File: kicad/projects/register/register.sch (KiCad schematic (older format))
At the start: 21 parts, among them J1 LEFT IN, J10 RIGHT LEDS, J2 LEFT OUT, J3 LEFT CONTENT, J4 BUS, J5 LEFT LEDS, J6 BACKPLANE, J7 RIGHT IN, J8 RIGHT OUT, J9 RIGHT CONTENT, U1 74HCT377, U2 74HCT245, U3 74HCT04, U4 74HCT377, U5 74HCT245

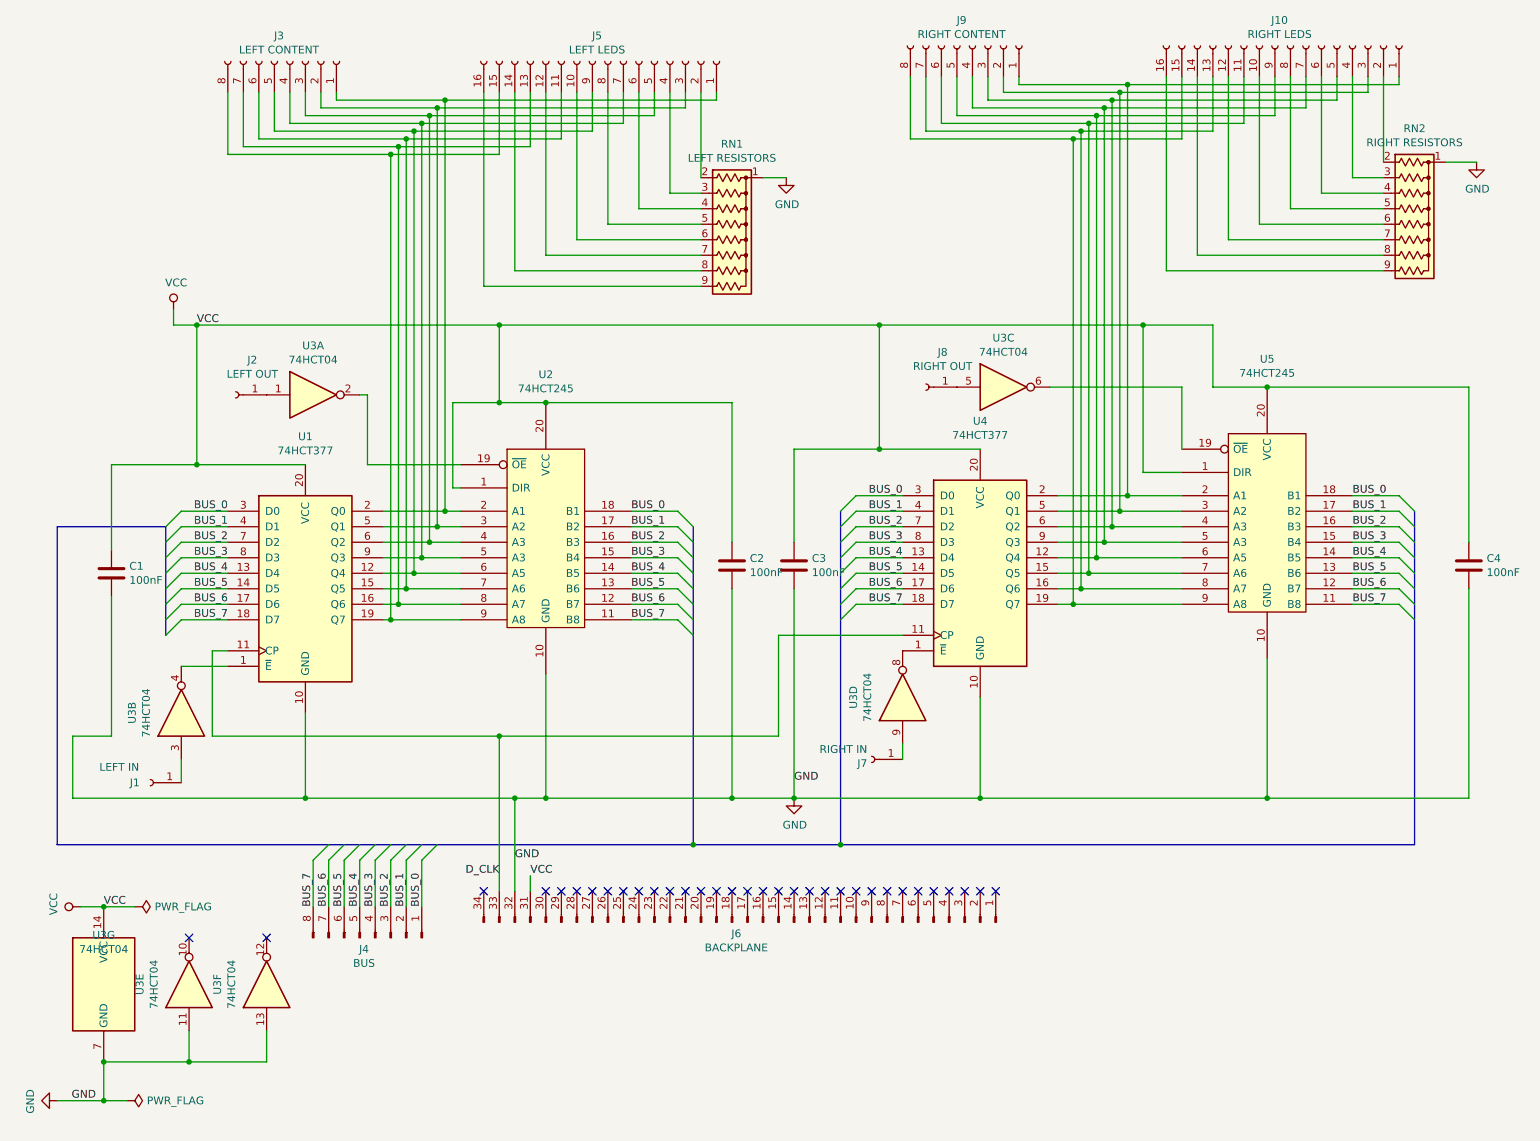
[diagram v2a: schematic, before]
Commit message: First version of register pcb. Ground and power planes giving poor results.
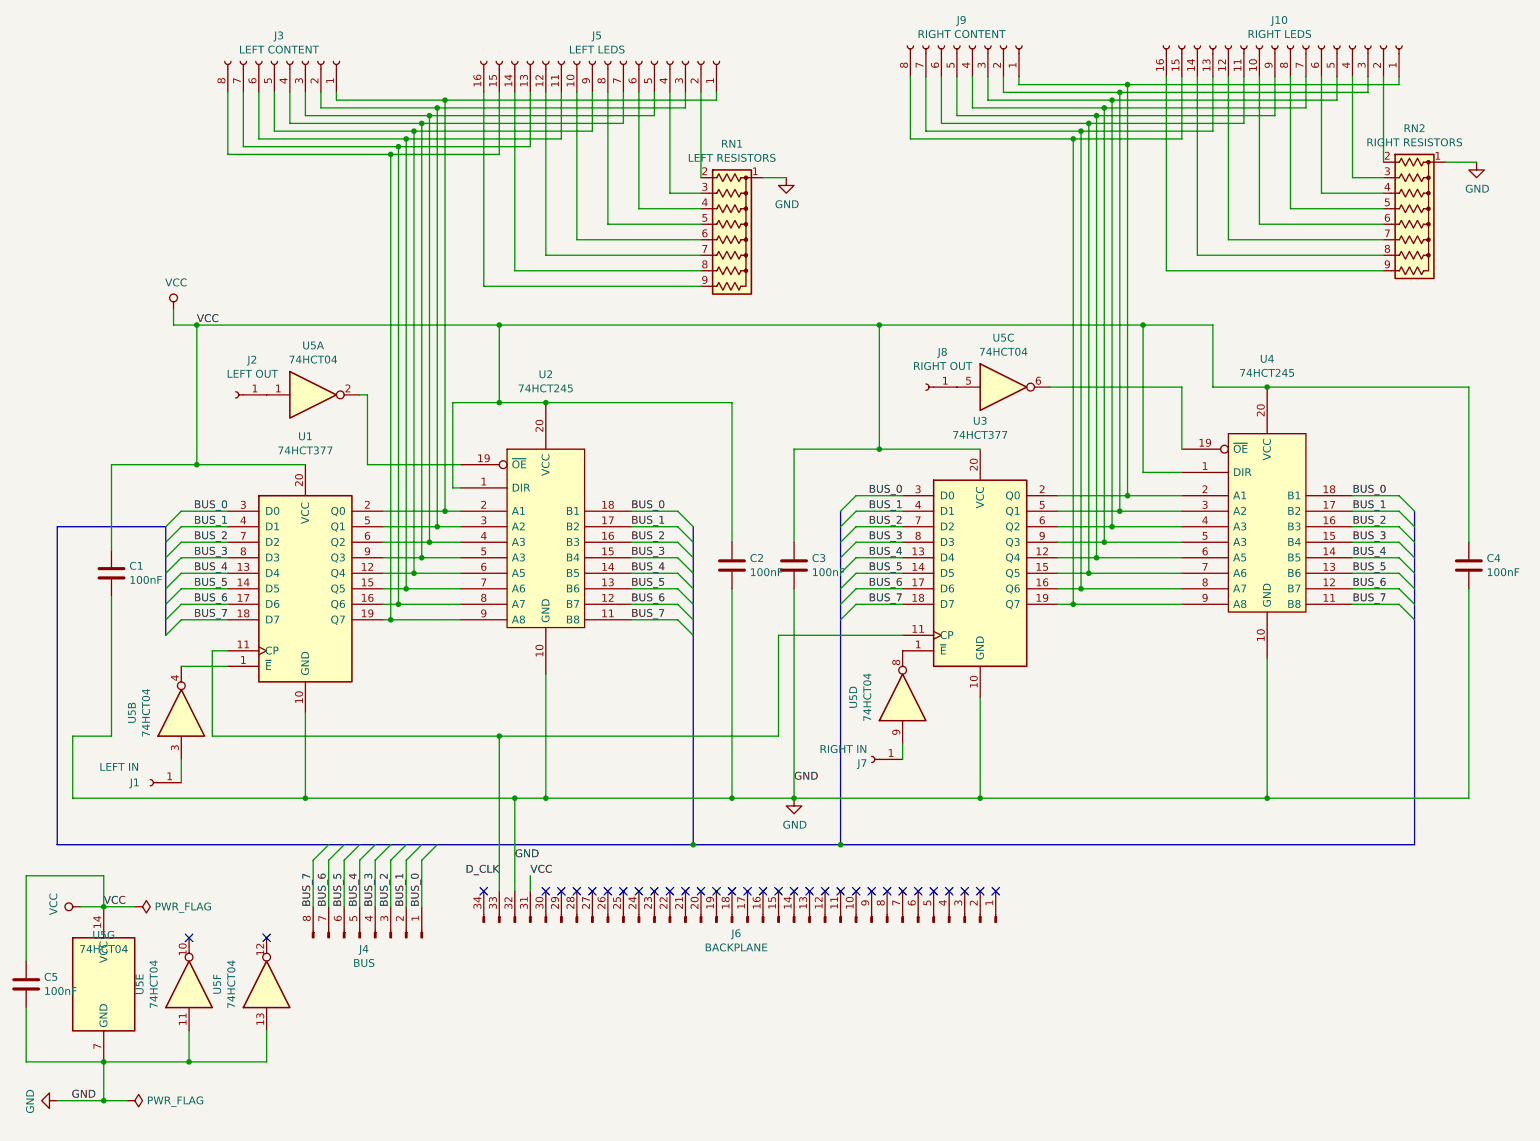
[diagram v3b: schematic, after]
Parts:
- added C5: 100nF, Capacitor_THT:C_Disc_D4.7mm_W2.5mm_P5.00mm, symbol Device:C
- J1, J2, J7, J8: footprint Connector_Wire:SolderWirePad_1x01_Drill1mm -> Connector_Wire:SolderWirePad_1x01_Drill0.8mm
- renumbered U4 to U3, U5 to U4, U3 to U5
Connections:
- net GND: now also C5.2
- net VCC: now also C5.1
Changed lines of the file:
@@
 $EndDescr
 $Comp
-L 74xx:74HCT04 U3
+L 74xx:74HCT04 U5
 U 3 1 5E0F9A71
 P 6950 3200
-F 0 "U3" H 6950 3517 50  0000 C CNN
+F 0 "U5" H 6950 3517 50  0000 C CNN
 F 1 "74HCT04" H 6950 3426 50  0000 C CNN
 F 2 "Package_DIP:DIP-14_W7.62mm_Socket" H 6950 3200 50  0001 C CNN
@@
 $EndComp
 $Comp
-L 74xx:74HCT04 U3
+L 74xx:74HCT04 U5
 U 1 1 5E0F8B7C
 P 2500 3250
-F 0 "U3" H 2500 3567 50  0000 C CNN
+F 0 "U5" H 2500 3567 50  0000 C CNN
 F 1 "74HCT04" H 2500 3476 50  0000 C CNN
 F 2 "Package_DIP:DIP-14_W7.62mm_Socket" H 2500 3250 50  0001 C CNN
@@
 F 0 "J1" H 1550 5750 50  0000 C CNN
 F 1 "LEFT IN" H 1650 5650 50  0000 C CNN
-F 2 "Connector_Wire:SolderWirePad_1x01_Drill1mm" H 1450 5750 50  0001 C CNN
+F 2 "Connector_Wire:SolderWirePad_1x01_Drill0.8mm" H 1450 5750 50  0001 C CNN
 F 3 "~" H 1450 5750 50  0001 C CNN
 	1    1450 5750
@@
 F 0 "J2" H 1892 3025 50  0000 C CNN
 F 1 "LEFT OUT" H 1892 3116 50  0000 C CNN
-F 2 "Connector_Wire:SolderWirePad_1x01_Drill1mm" H 2000 3250 50  0001 C CNN
+F 2 "Connector_Wire:SolderWirePad_1x01_Drill0.8mm" H 2000 3250 50  0001 C CNN
 F 3 "~" H 2000 3250 50  0001 C CNN
 	1    2000 3250
@@
 F 0 "J8" H 6342 2975 50  0000 C CNN
 F 1 "RIGHT OUT" H 6342 3066 50  0000 C CNN
-F 2 "Connector_Wire:SolderWirePad_1x01_Drill1mm" H 6450 3200 50  0001 C CNN
+F 2 "Connector_Wire:SolderWirePad_1x01_Drill0.8mm" H 6450 3200 50  0001 C CNN
 F 3 "~" H 6450 3200 50  0001 C CNN
 	1    6450 3200
@@
 F 0 "J7" H 6128 5626 50  0000 L CNN
 F 1 "RIGHT IN" H 6128 5535 50  0000 L CNN
-F 2 "Connector_Wire:SolderWirePad_1x01_Drill1mm" H 6100 5600 50  0001 C CNN
+F 2 "Connector_Wire:SolderWirePad_1x01_Drill0.8mm" H 6100 5600 50  0001 C CNN
 F 3 "~" H 6100 5600 50  0001 C CNN
 	1    6100 5600
@@
 	4550 4700 4850 4700
 $Comp
-L 74xx:74HCT04 U3
+L 74xx:74HCT04 U5
 U 2 1 5E424536
 P 1650 5300
-F 0 "U3" H 1650 5617 50  0000 C CNN
+F 0 "U5" H 1650 5617 50  0000 C CNN
 F 1 "74HCT04" H 1650 5526 50  0000 C CNN
 F 2 "Package_DIP:DIP-14_W7.62mm_Socket" H 1650 5300 50  0001 C CNN
@@
 $EndComp
 $Comp
-L 74xx:74HCT04 U3
+L 74xx:74HCT04 U5
 U 4 1 5E425697
 P 6300 5200
-F 0 "U3" H 6300 5517 50  0000 C CNN
+F 0 "U5" H 6300 5517 50  0000 C CNN
 F 1 "74HCT04" H 6300 5426 50  0000 C CNN
 F 2 "Package_DIP:DIP-14_W7.62mm_Socket" H 6300 5200 50  0001 C CNN
@@
 	4000 3300 5200 3300
 $Comp
-L eight-bit-computer:74HCT377 U4
+L eight-bit-computer:74HCT377 U3
 U 1 1 5E125DFF
 P 6800 4400
-F 0 "U4" H 6800 5381 50  0000 C CNN
+F 0 "U3" H 6800 5381 50  0000 C CNN
 F 1 "74HCT377" H 6800 5290 50  0000 C CNN
 F 2 "Package_DIP:DIP-20_W7.62mm_Socket" H 6800 4400 50  0001 C CNN
@@
 	8300 3200 8650 3200
 $Comp
-L eight-bit-computer:74HCT245 U5
+L eight-bit-computer:74HCT245 U4
 U 1 1 5E1273A1
 P 8650 4150
-F 0 "U5" H 8650 5281 50  0000 C CNN
+F 0 "U4" H 8650 5281 50  0000 C CNN
 F 1 "74HCT245" H 8650 5190 50  0000 C CNN
 F 2 "Package_DIP:DIP-20_W7.62mm_Socket" H 8300 4150 50  0001 C CNN
@@
 	3800 5850 4000 5850
 $Comp
-L 74xx:74HCT04 U3
+L 74xx:74HCT04 U5
 U 7 1 5E204B57
 P 1150 7050
-F 0 "U3" H 1150 7367 50  0000 C CNN
+F 0 "U5" H 1150 7367 50  0000 C CNN
 F 1 "74HCT04" H 1150 7276 50  0000 C CNN
 F 2 "Package_DIP:DIP-14_W7.62mm_Socket" H 1150 7050 50  0001 C CNN
@@
 $EndComp
 $Comp
-L 74xx:74HCT04 U3
+L 74xx:74HCT04 U5
 U 5 1 5E206221
 P 1700 7050
-F 0 "U3" H 1700 7367 50  0000 C CNN
+F 0 "U5" H 1700 7367 50  0000 C CNN
 F 1 "74HCT04" H 1700 7276 50  0000 C CNN
 F 2 "Package_DIP:DIP-14_W7.62mm_Socket" H 1700 7050 50  0001 C CNN
@@
 $EndComp
 $Comp
-L 74xx:74HCT04 U3
+L 74xx:74HCT04 U5
 U 6 1 5E2090E4
 P 2200 7050
-F 0 "U3" H 2200 7367 50  0000 C CNN
+F 0 "U5" H 2200 7367 50  0000 C CNN
 F 1 "74HCT04" H 2200 7276 50  0000 C CNN
 F 2 "Package_DIP:DIP-14_W7.62mm_Socket" H 2200 7050 50  0001 C CNN
@@
 Wire Wire Line
 	850  7800 1150 7800
+$Comp
+L Device:C C5
+U 1 1 5E152FC3
+P 650 7050
+F 0 "C5" H 765 7096 50  0000 L CNN
+F 1 "100nF" H 765 7005 50  0000 L CNN
+F 2 "Capacitor_THT:C_Disc_D4.7mm_W2.5mm_P5.00mm" H 688 6900 50  0001 C CNN
+F 3 "~" H 650 7050 50  0001 C CNN
+	1    650  7050
+	1    0    0    -1
+$EndComp
+Wire Wire Line
+	650  7200 650  7550
+Wire Wire Line
+	650  7550 1150 7550
+Wire Wire Line
+	650  6900 650  6350
+Wire Wire Line
+	650  6350 1150 6350
+Wire Wire Line
+	1150 6350 1150 6550
 Wire Bus Line
 	9600 4000 9600 6150

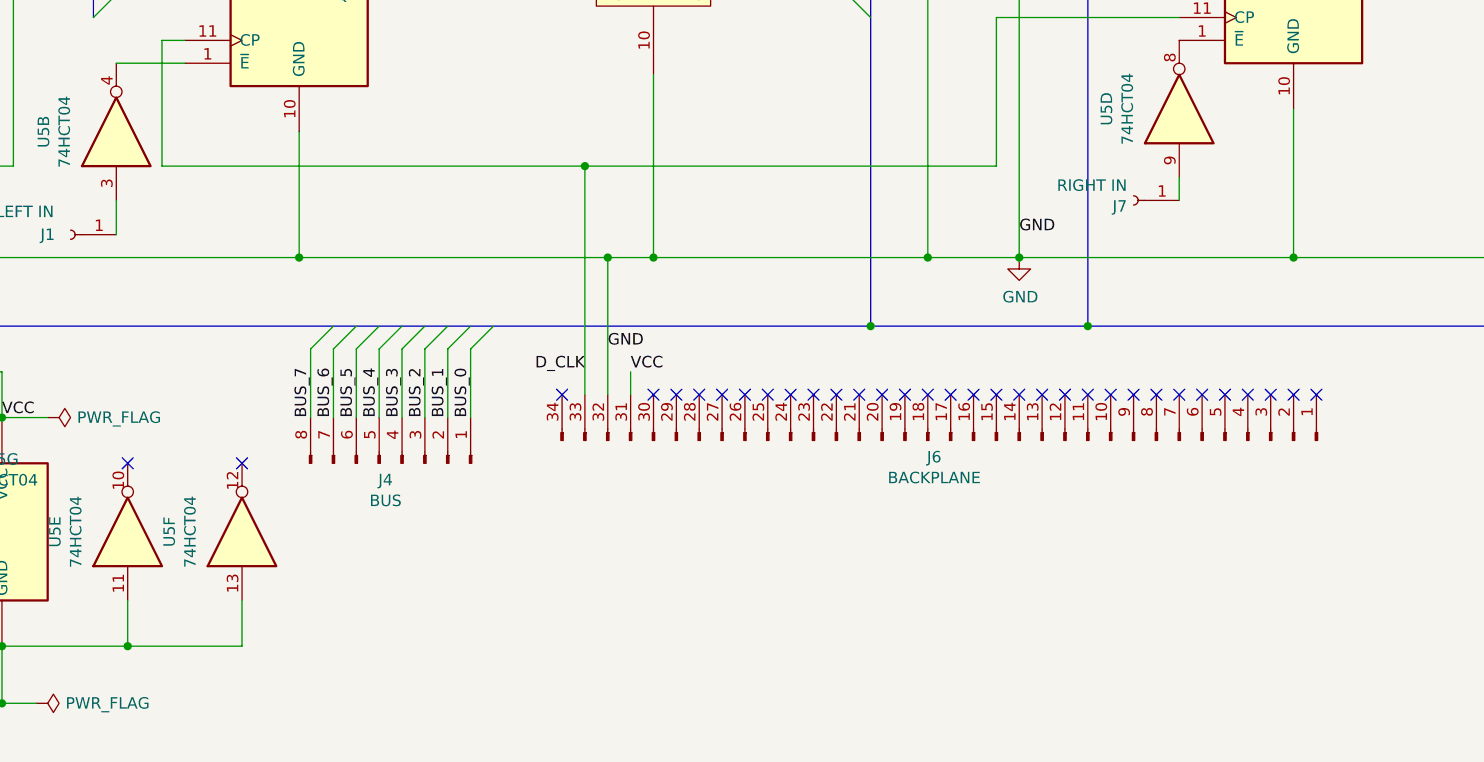
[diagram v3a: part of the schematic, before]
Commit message: Add bus and aux symbols. Update backplane footprint and 3dmodel. Update register PCB to use new footprints.
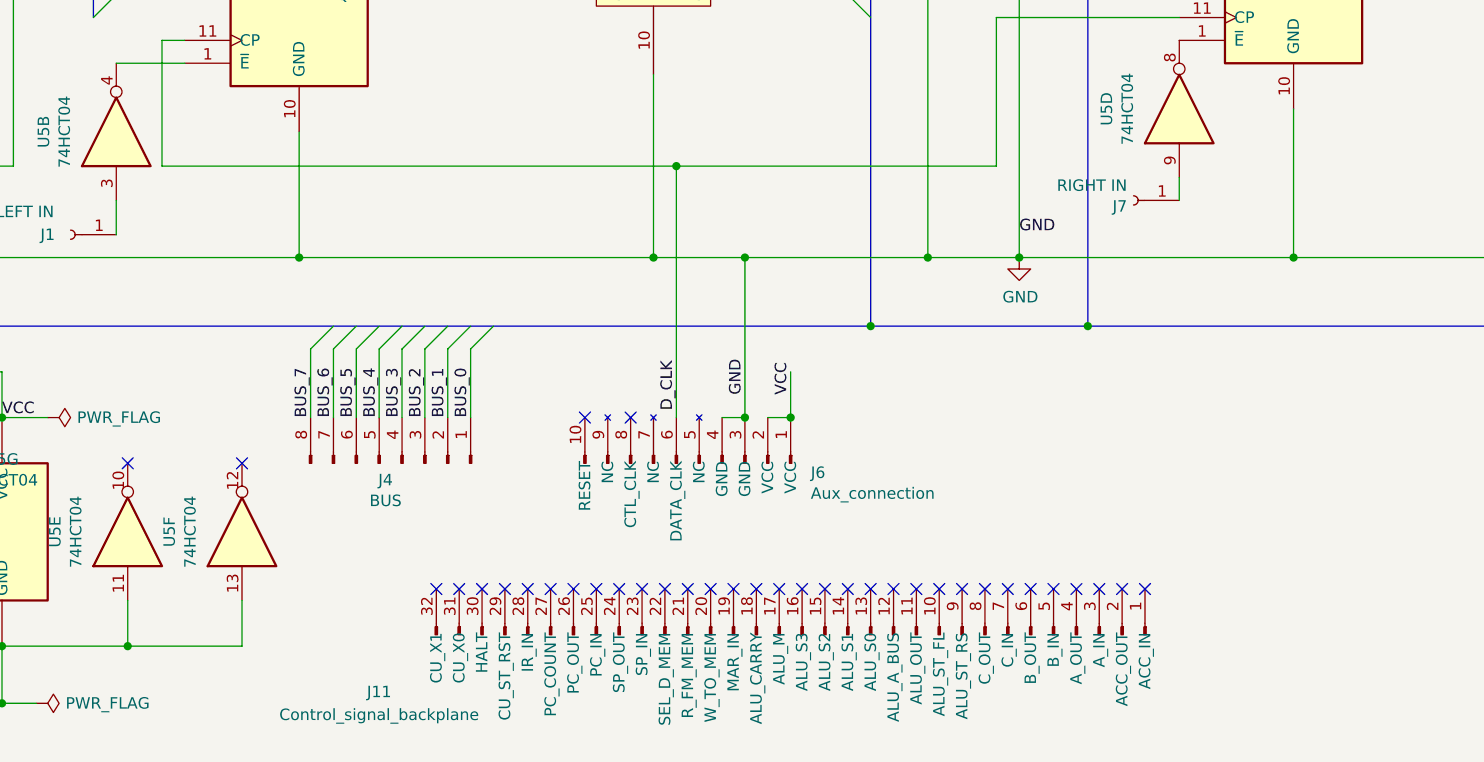
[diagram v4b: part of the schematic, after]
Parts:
- removed J6: BACKPLANE, eight-bit-computer:backplane-connector, symbol Connector:Conn_01x34_Male
- added J11: Control_signal_backplane, eight-bit-computer:backplane-connector, symbol eight-bit-computer:Control_signal_backplane
- added J6: Aux_connection, Connector_PinHeader_2.54mm:PinHeader_1x10_P2.54mm_Horizontal, symbol eight-bit-computer:Aux_connection
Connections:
- net D_CLK: now also J6.6 (DATA_CLK)
- net GND: now also J6.3 (GND), J6.4 (GND)
- net VCC: now also J6.1 (VCC), J6.2 (VCC)
- no-connect marks 33 -> 36
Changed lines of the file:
@@
 Wire Wire Line
 	1850 4900 1950 4900
-Connection ~ 3700 5450
 Wire Wire Line
 	1650 5000 1950 5000
 Wire Wire Line
-	1850 5450 3700 5450
-Wire Wire Line
 	1850 4900 1850 5450
 Wire Wire Line
 	2450 5300 2450 5850
-Wire Wire Line
-	2450 5850 3800 5850
 Wire Wire Line
 	8650 5850 8650 4950
@@
 	6300 5500 6300 5600
 Wire Wire Line
-	5600 4500 5600 5850
-Wire Wire Line
 	5500 4800 5500 5450
 Wire Wire Line
 	5500 4800 6300 4800
 Wire Wire Line
-	3700 5450 5500 5450
-Wire Wire Line
 	5200 3300 5200 4200
-Wire Wire Line
-	5200 4500 5200 5850
 Connection ~ 5200 5850
 Wire Wire Line
@@
 Wire Wire Line
 	8100 3200 8100 3600
-NoConn ~ 4100 6450
-NoConn ~ 4200 6450
-NoConn ~ 4300 6450
-NoConn ~ 4400 6450
-NoConn ~ 4500 6450
-NoConn ~ 4600 6450
-NoConn ~ 4700 6450
-NoConn ~ 4800 6450
-NoConn ~ 4900 6450
-NoConn ~ 5000 6450
-NoConn ~ 5100 6450
-NoConn ~ 5200 6450
-NoConn ~ 5300 6450
-NoConn ~ 5400 6450
-NoConn ~ 5500 6450
-NoConn ~ 5600 6450
-NoConn ~ 5700 6450
-NoConn ~ 5800 6450
-NoConn ~ 5900 6450
-NoConn ~ 6000 6450
-NoConn ~ 6100 6450
-NoConn ~ 6200 6450
-NoConn ~ 6300 6450
-NoConn ~ 6400 6450
-NoConn ~ 6500 6450
-NoConn ~ 6600 6450
-NoConn ~ 6700 6450
-NoConn ~ 6800 6450
-NoConn ~ 6900 6450
 Text Label 1750 2800 0    50   ~ 0
 VCC
-Text Label 3900 6350 0    50   ~ 0
+Text Label 4600 6450 1    50   ~ 0
 VCC
-Text Label 3800 6250 0    50   ~ 0
+Text Label 4400 6450 1    50   ~ 0
 GND
 Text Label 5600 5750 0    50   ~ 0
 GND
-$Comp
-L Connector:Conn_01x34_Male J6
-U 1 1 5E143442
-P 5300 6650
-F 0 "J6" V 5227 6578 50  0000 C CNN
-F 1 "BACKPLANE" V 5136 6578 50  0000 C CNN
-F 2 "eight-bit-computer:backplane-connector" H 5300 6650 50  0001 C CNN
-F 3 "~" H 5300 6650 50  0001 C CNN
-	1    5300 6650
-	0    1    -1   0
-$EndComp
-NoConn ~ 3600 6450
-Wire Wire Line
-	3700 5450 3700 6450
-NoConn ~ 4000 6450
-Text Label 3700 6350 2    50   ~ 0
+Text Label 4100 6300 3    50   ~ 0
 D_CLK
 Wire Wire Line
-	3900 6450 3900 6350
-Wire Wire Line
-	3800 5850 3800 6450
-Connection ~ 3800 5850
-Wire Wire Line
-	3800 5850 4000 5850
+	4600 6550 4600 6350
 $Comp
 L 74xx:74HCT04 U5
@@
 	1750 2800 3700 2800
 Wire Wire Line
-	4000 5850 5200 5850
+	4000 5850 4400 5850
 $Comp
 L power:PWR_FLAG #FLG0101
@@
 Wire Wire Line
 	1150 6350 1150 6550
+$Comp
+L eight-bit-computer:Control_signal_backplane J11
+U 1 1 5FD0DA26
+P 4650 7500
+F 0 "J11" V 4400 5650 50  0000 C CNN
+F 1 "Control_signal_backplane" V 4300 5650 50  0000 C CNN
+F 2 "eight-bit-computer:backplane-connector" H 4650 7500 50  0001 C CNN
+F 3 "~" H 4650 7500 50  0001 C CNN
+	1    4650 7500
+	0    1    -1   0
+$EndComp
+NoConn ~ 6150 7300
+NoConn ~ 6050 7300
+NoConn ~ 5950 7300
+NoConn ~ 5850 7300
+NoConn ~ 5750 7300
+NoConn ~ 5650 7300
+NoConn ~ 5550 7300
+NoConn ~ 5450 7300
+NoConn ~ 5350 7300
+NoConn ~ 5250 7300
+NoConn ~ 5150 7300
+NoConn ~ 5050 7300
+NoConn ~ 4950 7300
+NoConn ~ 4850 7300
+NoConn ~ 4750 7300
+NoConn ~ 4650 7300
+NoConn ~ 4550 7300
+NoConn ~ 4450 7300
+NoConn ~ 4350 7300
+NoConn ~ 4250 7300
+NoConn ~ 4150 7300
+NoConn ~ 4050 7300
+NoConn ~ 3950 7300
+NoConn ~ 3850 7300
+NoConn ~ 3750 7300
+NoConn ~ 3650 7300
+NoConn ~ 3550 7300
+NoConn ~ 3450 7300
+NoConn ~ 3350 7300
+NoConn ~ 3150 7300
+NoConn ~ 3050 7300
+$Comp
+L eight-bit-computer:Aux_connection J6
+U 1 1 6002EF1B
+P 4200 6750
+F 0 "J6" V 4159 7238 50  0000 L CNN
+F 1 "Aux_connection" V 4068 7238 50  0000 L CNN
+F 2 "Connector_PinHeader_2.54mm:PinHeader_1x10_P2.54mm_Horizontal" H 4200 6750 50  0001 C CNN
+F 3 "~" H 4200 6750 50  0001 C CNN
+	1    4200 6750
+	0    1    -1   0
+$EndComp
+NoConn ~ 3250 7300
+Wire Wire Line
+	4500 6550 4600 6550
+Connection ~ 4600 6550
+Wire Wire Line
+	4300 6550 4400 6550
+Wire Wire Line
+	4400 6550 4400 5850
+Connection ~ 4400 6550
+Connection ~ 4400 5850
+Wire Wire Line
+	4400 5850 5200 5850
+NoConn ~ 3700 6550
+NoConn ~ 3900 6550
+Wire Wire Line
+	4100 6550 4100 5450
+Connection ~ 4100 5450
+Wire Wire Line
+	4100 5450 5500 5450
+Wire Wire Line
+	1850 5450 4100 5450
+Wire Wire Line
+	2450 5850 4000 5850
+Wire Wire Line
+	5200 4500 5200 5850
+Wire Wire Line
+	5600 4500 5600 5850
 Wire Bus Line
 	9600 4000 9600 6150
